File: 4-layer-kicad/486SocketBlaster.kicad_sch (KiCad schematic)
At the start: 16 parts, among them U1 TPS563200

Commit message: update
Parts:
- added R4: 40.2K, 486SocketBlaster:R_0603_1608Metric, symbol Device:R
- added RV1: 100K, 486SocketBlaster:tinySMDpot, symbol Device:R_Potentiometer
- R2: value 33.2K -> 68K; JLCPCB C4216 -> (none); JLCPCB for set (none) -> C4216; Set valie (none) -> 33.2K; adj value (none) -> 68K
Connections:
- net FBVoltage: now also R4.1
- net Vout: now also RV1.1
- new net: R4.2, RV1.2
- no-connect marks 0 -> 1
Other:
- moved on the sheet: R2, R3

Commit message: update
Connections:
- net FBVoltage: now also R3.1; no longer R3.2
- net GND: now also R3.2; no longer R3.1
- net SW: now also C4.2; no longer C4.1
- net Vin: now also R1.2; no longer R1.1
- net Vout: now also RV1.3; no longer RV1.1
- net at U1.6 (VBST): now also C4.1; no longer C4.2
- net at U1.5 (EN): now also R1.1; no longer R1.2
- net Trim: now reaches R4.2, RV1.2
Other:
- moved on the sheet: C4, R1, R3, RV1
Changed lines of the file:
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@@
   (junction (at 488.95 63.5) (diameter 0) (color 0 0 0 0)
   )
+  (junction (at 233.68 153.67) (diameter 0) (color 0 0 0 0)
+  )
   (junction (at 285.75 63.5) (diameter 0) (color 0 0 0 0)
   )
@@
   (junction (at 318.77 63.5) (diameter 0) (color 0 0 0 0)
   )
-  (junction (at 162.56 175.26) (diameter 0) (color 0 0 0 0)
-  )
   (junction (at 483.87 63.5) (diameter 0) (color 0 0 0 0)
   )
@@
   (junction (at 236.22 38.1) (diameter 0) (color 0 0 0 0)
   )
-  (junction (at 163.83 153.67) (diameter 0) (color 0 0 0 0)
-  )
   (junction (at 120.65 158.75) (diameter 0) (color 0 0 0 0)
   )
@@
   )
   (junction (at 336.55 88.9) (diameter 0) (color 0 0 0 0)
-  )
-  (junction (at 233.68 153.67) (diameter 0) (color 0 0 0 0)
   )
   (junction (at 448.31 88.9) (diameter 0) (color 0 0 0 0)
@@
     (stroke (width 0) (type default) (color 0 0 0 0))
   )
-  (wire (pts (xy 162.56 175.26) (xy 162.56 177.8))
-    (stroke (width 0) (type default) (color 0 0 0 0))
-  )
   (wire (pts (xy 499.11 63.5) (xy 514.35 63.5))
     (stroke (width 0) (type default) (color 0 0 0 0))
@@
     (stroke (width 0) (type default) (color 0 0 0 0))
   )
-  (wire (pts (xy 163.83 151.13) (xy 163.83 153.67))
-    (stroke (width 0) (type default) (color 0 0 0 0))
-  )
   (wire (pts (xy 229.87 57.15) (xy 229.87 53.34))
     (stroke (width 0) (type default) (color 0 0 0 0))
@@
     (stroke (width 0) (type default) (color 0 0 0 0))
   )
+  (wire (pts (xy 233.68 153.67) (xy 241.3 153.67))
+    (stroke (width 0) (type default) (color 0 0 0 0))
+  )
   (wire (pts (xy 146.05 88.9) (xy 151.13 88.9))
     (stroke (width 0) (type default) (color 0 0 0 0))
@@
   )
   (wire (pts (xy 335.28 57.15) (xy 336.55 57.15))
-    (stroke (width 0) (type default) (color 0 0 0 0))
-  )
-  (wire (pts (xy 233.68 153.67) (xy 241.3 153.67))
     (stroke (width 0) (type default) (color 0 0 0 0))
   )
@@
   (text "3AMP Step Down Coverter" (at 139.7 143.51 0)
     (effects (font (size 1.27 1.27)) (justify left bottom))
+  )
+  (label "FBVoltage" (at 165.1 175.26 0)
+    (effects (font (size 1.27 1.27)) (justify left bottom))
+  )
+  (label "SW" (at 163.83 153.67 0)
+    (effects (font (size 1.27 1.27)) (justify left bottom))
+  )
+  (label "Trim" (at 222.25 157.48 0)
+    (effects (font (size 1 1)) (justify left bottom))
   )
   (global_label "Vout" (shape input) (at 241.3 153.67 0) (fields_autoplaced)
@@
     )
   )
-  (global_label "SW" (shape input) (at 163.83 151.13 0) (fields_autoplaced)
-    (effects (font (size 1.27 1.27)) (justify left))
-    (property "Intersheet References" "${INTERSHEET_REFS}" (id 0) (at 168.9041 151.0506 0)
-      (effects (font (size 1.27 1.27)) (justify left) hide)
-    )
-  )
   (global_label "Vin" (shape input) (at 90.17 158.75 180) (fields_autoplaced)
     (effects (font (size 1.27 1.27)) (justify right))
@@
     (effects (font (size 1.27 1.27)) (justify left))
     (property "Intersheet References" "${INTERSHEET_REFS}" (id 0) (at 303.6166 30.4006 0)
-      (effects (font (size 1.27 1.27)) (justify left) hide)
-    )
-  )
-  (global_label "FBVoltage" (shape input) (at 162.56 177.8 0) (fields_autoplaced)
-    (effects (font (size 1.27 1.27)) (justify left))
-    (property "Intersheet References" "${INTERSHEET_REFS}" (id 0) (at 174.3469 177.7206 0)
       (effects (font (size 1.27 1.27)) (justify left) hide)
     )
@@
     (pin "3")
   )
-  (symbol (lib_id "Device:C") (at 168.91 161.29 270) (unit 1)
+  (symbol (lib_id "Device:C") (at 168.91 161.29 90) (unit 1)
     (in_bom yes) (on_board yes)
-    (property "Reference" "C4" (id 0) (at 168.91 165.1 90))
-    (property "Value" "0.1uf" (id 1) (at 168.91 157.48 90))
-    (property "Footprint" "486SocketBlaster:C_0603_1608Metric" (id 2) (at 165.1 162.2552 0)
+    (property "Reference" "C4" (id 0) (at 168.91 157.48 90))
+    (property "Value" "0.1uf" (id 1) (at 168.91 165.1 90))
+    (property "Footprint" "486SocketBlaster:C_0603_1608Metric" (id 2) (at 172.72 160.3248 0)
       (effects (font (size 1.27 1.27)) hide)
     )
@@
     (pin "2")
   )
-  (symbol (lib_id "Device:R") (at 137.16 163.83 90) (unit 1)
+  (symbol (lib_id "Device:R") (at 137.16 163.83 270) (unit 1)
     (in_bom yes) (on_board yes)
-    (property "Reference" "R1" (id 0) (at 137.16 161.29 90))
+    (property "Reference" "R1" (id 0) (at 137.16 166.37 90))
     (property "Value" "10K" (id 1) (at 137.16 163.83 90))
-    (property "Footprint" "486SocketBlaster:R_0603_1608Metric" (id 2) (at 137.16 165.608 90)
+    (property "Footprint" "486SocketBlaster:R_0603_1608Metric" (id 2) (at 137.16 162.052 90)
       (effects (font (size 1.27 1.27)) hide)
     )
@@
     (pin "2")
   )
-  (symbol (lib_id "Device:R_Potentiometer") (at 233.68 157.48 0) (mirror y) (unit 1)
+  (symbol (lib_id "Device:R_Potentiometer") (at 233.68 157.48 180) (unit 1)
     (in_bom yes) (on_board yes) (fields_autoplaced)
     (property "Reference" "RV1" (id 0) (at 236.22 156.2099 0)
@@
     (pin "1")
   )
-  (symbol (lib_id "Device:R") (at 212.09 172.72 180) (unit 1)
+  (symbol (lib_id "Device:R") (at 212.09 172.72 0) (unit 1)
     (in_bom yes) (on_board yes)
-    (property "Reference" "R3" (id 0) (at 209.55 172.72 90))
+    (property "Reference" "R3" (id 0) (at 214.63 172.72 90))
     (property "Value" "10K" (id 1) (at 212.09 172.72 90))
-    (property "Footprint" "486SocketBlaster:R_0603_1608Metric" (id 2) (at 213.868 172.72 90)
-      (effects (font (size 1.27 1.27)) hide)
-    )
+    (property "Footprint" "486SocketBlaster:R_0603_1608Metric" (id 2) (at 210.312 172.72 90)
+      (effects (font (size 1.27 1.27)) hide)
+    )

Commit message: added gerbers
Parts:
- R2: value 68K -> 68.1K; JLCPCB for ADJ (none) -> C25976
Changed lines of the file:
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@@
     (in_bom yes) (on_board yes)
     (property "Reference" "R2" (id 0) (at 209.55 157.48 90))
-    (property "Value" "68K" (id 1) (at 212.09 157.48 90)
+    (property "Value" "68.1K" (id 1) (at 212.09 157.48 90)
       (effects (font (size 1 1)))
     )
@@
       (effects (font (size 1.27 1.27)) hide)
     )
-    (property "JLCPCB for ADJ" "" (id 5) (at 212.09 157.48 90)
+    (property "JLCPCB for ADJ" "C25976" (id 5) (at 212.09 157.48 90)
       (effects (font (size 1.27 1.27)) hide)
     )
@@
     )
     (path "/26999f04-d342-4b3a-88f4-2c5731d20c32"
-      (reference "R2") (unit 1) (value "68K") (footprint "486SocketBlaster:R_0603_1608Metric")
+      (reference "R2") (unit 1) (value "68.1K") (footprint "486SocketBlaster:R_0603_1608Metric")
     )
     (path "/fd390462-f858-4bcd-808a-4e3a47d7079c"

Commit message: update
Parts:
- removed C7: 47uf, 486SocketBlaster:CP_EIA-3216-12_Kemet-S_Pad1.58x1.35mm_HandSolder, symbol Device:C_Polarized_Small
- added C7, C8: 10uf, 486SocketBlaster:C_0805_2012Metric, symbol Device:C_Small
- C3, C4: footprint 486SocketBlaster:C_0603_1608Metric -> 486SocketBlaster:C_0805_2012Metric
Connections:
- net GND: now also C7.2, C8.2
- net Vout: now also C7.1, C8.1
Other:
- moved on the sheet: C5, C6, R2, R3, R4, RV1

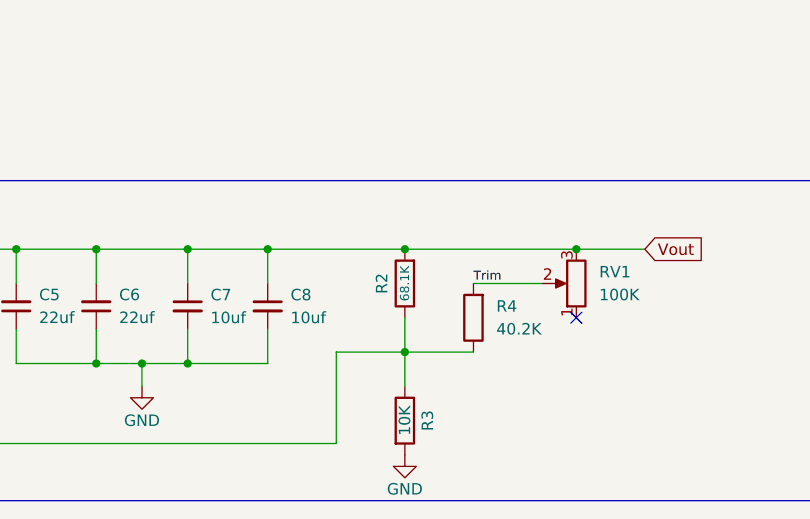
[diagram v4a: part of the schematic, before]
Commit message: update
+larger drill holes for socket
+Replaced 68.1K with 68K resistor, one less extended part from jlc
+updated gerbers, Bom & CPL
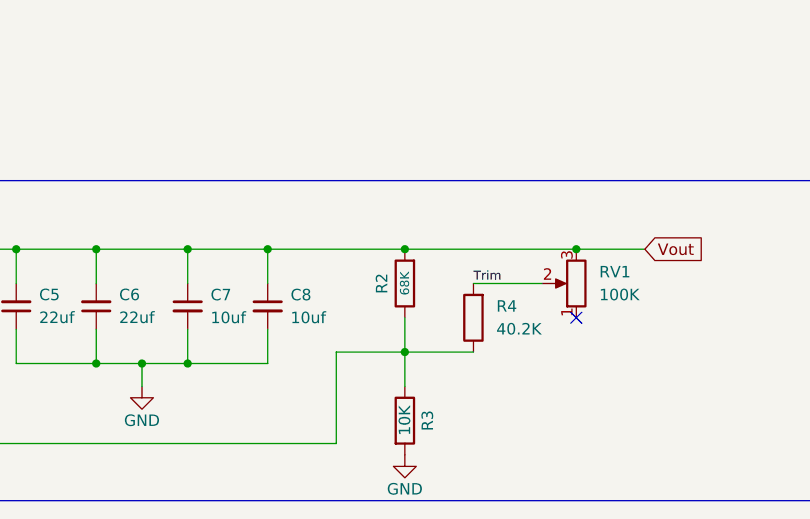
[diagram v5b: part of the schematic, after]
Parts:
- C3, C4: JLCPCB C28233 -> C49678
- C7, C8: JLCPCB C12891 -> C15850
- R2: value 68.1K -> 68K; JLCPCB for ADJ C25976 -> C23231
- RV1: JLCPCB (none) -> C719186; JLCPCB2 (none) -> C128545
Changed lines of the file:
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@@
       (effects (font (size 1.27 1.27)) hide)
     )
-    (property "JLCPCB" "C28233" (id 4) (at 168.91 161.29 90)
+    (property "JLCPCB" "C49678" (id 4) (at 168.91 161.29 90)
       (effects (font (size 1.27 1.27)) hide)
     )
@@
     (in_bom yes) (on_board yes)
     (property "Reference" "R2" (id 0) (at 224.79 157.48 90))
-    (property "Value" "68.1K" (id 1) (at 227.33 157.48 90)
+    (property "Value" "68K" (id 1) (at 227.33 157.48 90)
       (effects (font (size 1 1)))
     )
@@
       (effects (font (size 1.27 1.27)) hide)
     )
-    (property "JLCPCB for ADJ" "C25976" (id 5) (at 227.33 157.48 90)
+    (property "JLCPCB for ADJ" "C23231" (id 5) (at 227.33 157.48 90)
       (effects (font (size 1.27 1.27)) hide)
     )
@@
       (effects (font (size 1.27 1.27)) hide)
     )
-    (property "JLCPCB" "C28233" (id 4) (at 120.65 162.56 0)
+    (property "JLCPCB" "C49678" (id 4) (at 120.65 162.56 0)
       (effects (font (size 1.27 1.27)) hide)
     )
@@
       (effects (font (size 1.27 1.27)) hide)
     )
+    (property "JLCPCB" "C719186" (id 4) (at 246.38 157.48 0)
+      (effects (font (size 1.27 1.27)) hide)
+    )
+    (property "JLCPCB2" "C128545" (id 5) (at 246.38 157.48 0)
+      (effects (font (size 1.27 1.27)) hide)
+    )
     (pin "1")
     (pin "2")
@@
       (effects (font (size 1.27 1.27)) hide)
     )
-    (property "JLCPCB" "C12891" (id 4) (at 203.2 160.02 0)
+    (property "JLCPCB" "C15850" (id 4) (at 203.2 160.02 0)
       (effects (font (size 1.27 1.27)) hide)
     )
@@
       (effects (font (size 1.27 1.27)) hide)
     )
-    (property "JLCPCB" "C12891" (id 4) (at 212.09 160.02 0)
+    (property "JLCPCB" "C15850" (id 4) (at 212.09 160.02 0)
       (effects (font (size 1.27 1.27)) hide)
     )
@@
     )
     (path "/26999f04-d342-4b3a-88f4-2c5731d20c32"
-      (reference "R2") (unit 1) (value "68.1K") (footprint "486SocketBlaster:R_0603_1608Metric")
+      (reference "R2") (unit 1) (value "68K") (footprint "486SocketBlaster:R_0603_1608Metric")
     )
     (path "/fd390462-f858-4bcd-808a-4e3a47d7079c"
